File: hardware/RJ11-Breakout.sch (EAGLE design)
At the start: 5 parts

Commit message: Added gear, version, dimensions, mounting holes with v-score.
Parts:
- added H2: STAND-OFF, SparkFun-Electromechanical:STAND-OFF
- added LOGO3: OSHW-LOGOMINI, SparkFun-Aesthetics:OSHW-LOGOMINI
- FRAME2: value (none) -> FRAME-LETTER
- JP2: value (none) -> Pins
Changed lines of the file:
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@@
 <?xml version="1.0" encoding="utf-8"?>
 <!DOCTYPE eagle SYSTEM "eagle.dtd">
-<eagle version="7.1.0">
+<eagle version="7.6.0">
 <drawing>
 <settings>
@@
 <grid distance="0.1" unitdist="inch" unit="inch" style="lines" multiple="1" display="no" altdistance="0.01" altunitdist="inch" altunit="inch"/>
 <layers>
-<layer number="1" name="Top" color="4" fill="1" visible="yes" active="no"/>
-<layer number="2" name="Route2" color="1" fill="3" visible="yes" active="no"/>
-<layer number="3" name="Route3" color="4" fill="3" visible="yes" active="no"/>
-<layer number="4" name="Route4" color="1" fill="4" visible="yes" active="no"/>
-<layer number="5" name="Route5" color="4" fill="4" visible="yes" active="no"/>
-<layer number="6" name="Route6" color="1" fill="8" visible="yes" active="no"/>
-<layer number="7" name="Route7" color="4" fill="8" visible="yes" active="no"/>
-<layer number="8" name="Route8" color="1" fill="2" visible="yes" active="no"/>
-<layer number="9" name="Route9" color="4" fill="2" visible="yes" active="no"/>
-<layer number="10" name="Route10" color="1" fill="7" visible="yes" active="no"/>
-<layer number="11" name="Route11" color="4" fill="7" visible="yes" active="no"/>
-<layer number="12" name="Route12" color="1" fill="5" visible="yes" active="no"/>
-<layer number="13" name="Route13" color="4" fill="5" visible="yes" active="no"/>
-<layer number="14" name="Route14" color="1" fill="6" visible="yes" active="no"/>
-<layer number="15" name="Route15" color="4" fill="6" visible="yes" active="no"/>
-<layer number="16" name="Bottom" color="1" fill="1" visible="yes" active="no"/>
-<layer number="17" name="Pads" color="2" fill="1" visible="yes" active="no"/>
-<layer number="18" name="Vias" color="2" fill="1" visible="yes" active="no"/>
-<layer number="19" name="Unrouted" color="6" fill="1" visible="yes" active="no"/>
-<layer number="20" name="Dimension" color="15" fill="1" visible="yes" active="no"/>
-<layer number="21" name="tPlace" color="16" fill="1" visible="yes" active="no"/>
-<layer number="22" name="bPlace" color="14" fill="1" visible="yes" active="no"/>
-<layer number="23" name="tOrigins" color="15" fill="1" visible="yes" active="no"/>
-<layer number="24" name="bOrigins" color="15" fill="1" visible="yes" active="no"/>
-<layer number="25" name="tNames" color="7" fill="1" visible="yes" active="no"/>
-<layer number="26" name="bNames" color="7" fill="1" visible="yes" active="no"/>
-<layer number="27" name="tValues" color="7" fill="1" visible="yes" active="no"/>
-<layer number="28" name="bValues" color="7" fill="1" visible="yes" active="no"/>
+<layer number="1" name="Top" color="4" fill="1" visible="no" active="no"/>
+<layer number="2" name="Route2" color="1" fill="3" visible="no" active="no"/>
+<layer number="3" name="Route3" color="4" fill="3" visible="no" active="no"/>
+<layer number="4" name="Route4" color="1" fill="4" visible="no" active="no"/>
+<layer number="5" name="Route5" color="4" fill="4" visible="no" active="no"/>
+<layer number="6" name="Route6" color="1" fill="8" visible="no" active="no"/>
+<layer number="7" name="Route7" color="4" fill="8" visible="no" active="no"/>
+<layer number="8" name="Route8" color="1" fill="2" visible="no" active="no"/>
+<layer number="9" name="Route9" color="4" fill="2" visible="no" active="no"/>
+<layer number="10" name="Route10" color="1" fill="7" visible="no" active="no"/>
+<layer number="11" name="Route11" color="4" fill="7" visible="no" active="no"/>
+<layer number="12" name="Route12" color="1" fill="5" visible="no" active="no"/>
+<layer number="13" name="Route13" color="4" fill="5" visible="no" active="no"/>
+<layer number="14" name="Route14" color="1" fill="6" visible="no" active="no"/>
+<layer number="15" name="Route15" color="4" fill="6" visible="no" active="no"/>
+<layer number="16" name="Bottom" color="1" fill="1" visible="no" active="no"/>
+<layer number="17" name="Pads" color="2" fill="1" visible="no" active="no"/>
+<layer number="18" name="Vias" color="2" fill="1" visible="no" active="no"/>
+<layer number="19" name="Unrouted" color="6" fill="1" visible="no" active="no"/>
+<layer number="20" name="Dimension" color="15" fill="1" visible="no" active="no"/>
+<layer number="21" name="tPlace" color="16" fill="1" visible="no" active="no"/>
+<layer number="22" name="bPlace" color="14" fill="1" visible="no" active="no"/>
+<layer number="23" name="tOrigins" color="15" fill="1" visible="no" active="no"/>
+<layer number="24" name="bOrigins" color="15" fill="1" visible="no" active="no"/>
+<layer number="25" name="tNames" color="7" fill="1" visible="no" active="no"/>
+<layer number="26" name="bNames" color="7" fill="1" visible="no" active="no"/>
+<layer number="27" name="tValues" color="7" fill="1" visible="no" active="no"/>
+<layer number="28" name="bValues" color="7" fill="1" visible="no" active="no"/>
 <layer number="29" name="tStop" color="7" fill="3" visible="no" active="no"/>
 <layer number="30" name="bStop" color="7" fill="6" visible="no" active="no"/>
@@
 <layer number="35" name="tGlue" color="7" fill="4" visible="no" active="no"/>
 <layer number="36" name="bGlue" color="7" fill="5" visible="no" active="no"/>
-<layer number="37" name="tTest" color="7" fill="1" visible="yes" active="no"/>
-<layer number="38" name="bTest" color="7" fill="1" visible="yes" active="no"/>
+<layer number="37" name="tTest" color="7" fill="1" visible="no" active="no"/>
+<layer number="38" name="bTest" color="7" fill="1" visible="no" active="no"/>
 <layer number="39" name="tKeepout" color="4" fill="11" visible="no" active="no"/>
 <layer number="40" name="bKeepout" color="1" fill="11" visible="no" active="no"/>
@@
 <layer number="44" name="Drills" color="7" fill="1" visible="no" active="no"/>
 <layer number="45" name="Holes" color="7" fill="1" visible="no" active="no"/>
-<layer number="46" name="Milling" color="3" fill="1" visible="yes" active="no"/>
-<layer number="47" name="Measures" color="7" fill="1" visible="yes" active="no"/>
-<layer number="48" name="Document" color="7" fill="1" visible="yes" active="no"/>
-<layer number="49" name="Reference" color="7" fill="1" visible="yes" active="no"/>
-<layer number="50" name="dxf" color="7" fill="1" visible="yes" active="no"/>
-<layer number="51" name="tDocu" color="6" fill="1" visible="yes" active="no"/>
-<layer number="52" name="bDocu" color="7" fill="1" visible="yes" active="no"/>
-<layer number="53" name="tGND_GNDA" color="7" fill="9" visible="yes" active="no"/>
-<layer number="54" name="bGND_GNDA" color="1" fill="9" visible="yes" active="no"/>
-<layer number="56" name="wert" color="7" fill="1" visible="yes" active="no"/>
-<layer number="57" name="tCAD" color="7" fill="1" visible="yes" active="no"/>
-<layer number="59" name="tCarbon" color="7" fill="1" visible="yes" active="no"/>
-<layer number="60" name="bCarbon" color="7" fill="1" visible="yes" active="no"/>
+<layer number="46" name="Milling" color="3" fill="1" visible="no" active="no"/>
+<layer number="47" name="Measures" color="7" fill="1" visible="no" active="no"/>
+<layer number="48" name="Document" color="7" fill="1" visible="no" active="no"/>
+<layer number="49" name="Reference" color="7" fill="1" visible="no" active="no"/>
+<layer number="50" name="dxf" color="7" fill="1" visible="no" active="no"/>
+<layer number="51" name="tDocu" color="6" fill="1" visible="no" active="no"/>
+<layer number="52" name="bDocu" color="7" fill="1" visible="no" active="no"/>
+<layer number="53" name="tGND_GNDA" color="7" fill="9" visible="no" active="no"/>
+<layer number="54" name="bGND_GNDA" color="1" fill="9" visible="no" active="no"/>
+<layer number="56" name="wert" color="7" fill="1" visible="no" active="no"/>
+<layer number="57" name="tCAD" color="7" fill="1" visible="no" active="no"/>
+<layer number="59" name="tCarbon" color="7" fill="1" visible="no" active="no"/>
+<layer number="60" name="bCarbon" color="7" fill="1" visible="no" active="no"/>
 <layer number="90" name="Modules" color="7" fill="1" visible="yes" active="yes"/>
 <layer number="91" name="Nets" color="2" fill="1" visible="yes" active="yes"/>
@@
 <layer number="112" name="tSilk" color="7" fill="1" visible="yes" active="yes"/>
 <layer number="113" name="IDFDebug" color="7" fill="1" visible="yes" active="yes"/>
+<layer number="114" name="Badge_Outline" color="7" fill="1" visible="yes" active="yes"/>
+<layer number="115" name="ReferenceISLANDS" color="7" fill="1" visible="yes" active="yes"/>
 <layer number="116" name="Patch_BOT" color="9" fill="4" visible="yes" active="yes"/>
+<layer number="118" name="Rect_Pads" color="7" fill="1" visible="yes" active="yes"/>
 <layer number="121" name="_tsilk" color="7" fill="1" visible="yes" active="yes"/>
 <layer number="122" name="_bsilk" color="7" fill="1" visible="yes" active="yes"/>
@@
 <part name="JP1" library="SparkFun-Connectors" deviceset="RJ11-6" device="PTH" value="RJ11"/>
 <part name="FRAME2" library="SparkFun-Aesthetics" deviceset="FRAME-LETTER" device=""/>
-<part name="JP2" library="SparkFun-Connectors" deviceset="M06" device="SILK_FEMALE_PTH"/>
+<part name="JP2" library="SparkFun-Connectors" deviceset="M06" device="SILK_FEMALE_PTH" value="Pins"/>
 <part name="LOGO1" library="SparkFun-Aesthetics" deviceset="SFE_LOGO_NAME_FLAME" device=".1_INCH"/>
 <part name="LOGO2" library="SparkFun-Aesthetics" deviceset="SFE_LOGO_NAME_FLAME" device=".1_INCH"/>
+<part name="LOGO3" library="SparkFun-Aesthetics" deviceset="OSHW-LOGO" device="MINI"/>
+<part name="H2" library="SparkFun-Electromechanical" deviceset="STAND-OFF" device=""/>
 </parts>
 <sheets>
@@
 <instance part="LOGO1" gate="G$1" x="86.36" y="2.54"/>
 <instance part="LOGO2" gate="G$1" x="86.36" y="2.54"/>
+<instance part="LOGO3" gate="G$1" x="68.58" y="12.7"/>
+<instance part="H2" gate="G$1" x="238.76" y="40.64"/>
 </instances>
 <busses>

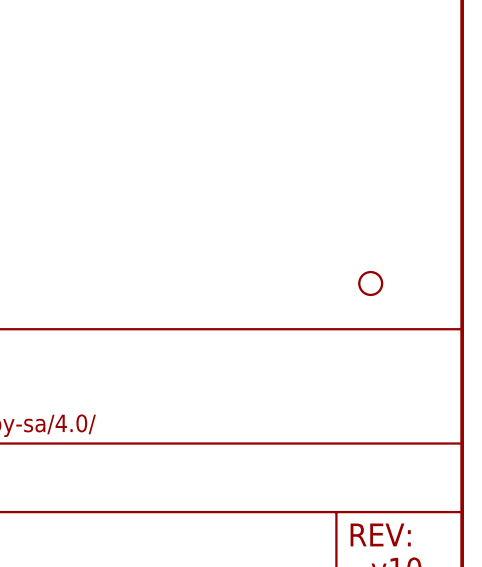
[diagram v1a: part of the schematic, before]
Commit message: Fixes to address issue 1
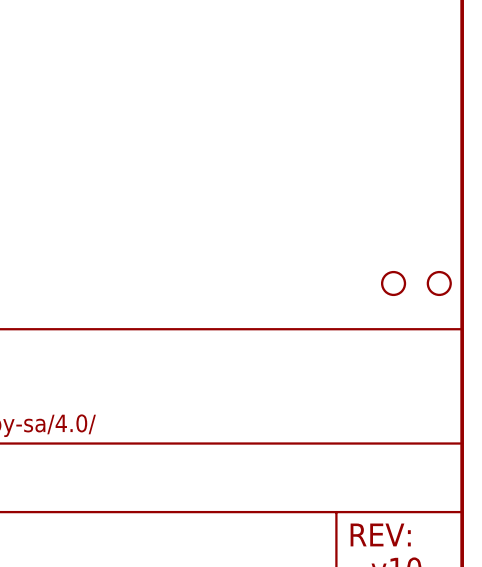
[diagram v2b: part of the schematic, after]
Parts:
- removed H2: STAND-OFF, SparkFun-Electromechanical:STAND-OFF
- added H1, H3: STAND-OFF, SparkFun-Electromechanical:STAND-OFF
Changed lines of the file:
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@@
 <part name="LOGO2" library="SparkFun-Aesthetics" deviceset="SFE_LOGO_NAME_FLAME" device=".1_INCH"/>
 <part name="LOGO3" library="SparkFun-Aesthetics" deviceset="OSHW-LOGO" device="MINI"/>
-<part name="H2" library="SparkFun-Electromechanical" deviceset="STAND-OFF" device=""/>
+<part name="H1" library="SparkFun-Electromechanical" deviceset="STAND-OFF" device=""/>
+<part name="H3" library="SparkFun-Electromechanical" deviceset="STAND-OFF" device=""/>
 </parts>
 <sheets>
@@
 <instance part="LOGO2" gate="G$1" x="86.36" y="2.54"/>
 <instance part="LOGO3" gate="G$1" x="68.58" y="12.7"/>
-<instance part="H2" gate="G$1" x="238.76" y="40.64"/>
+<instance part="H1" gate="G$1" x="246.38" y="40.64"/>
+<instance part="H3" gate="G$1" x="241.3" y="40.64"/>
 </instances>
 <busses>
